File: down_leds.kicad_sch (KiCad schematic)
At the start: 9 parts, among them U5 DMG2305UX-7

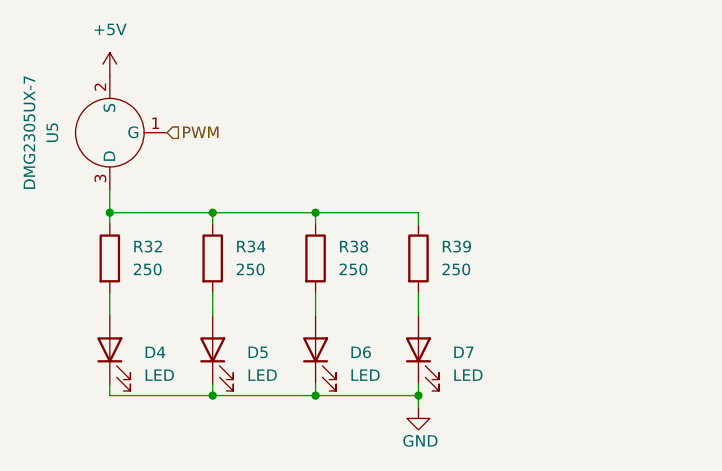
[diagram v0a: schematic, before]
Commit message: finished wiring motor drivers and moved boot button
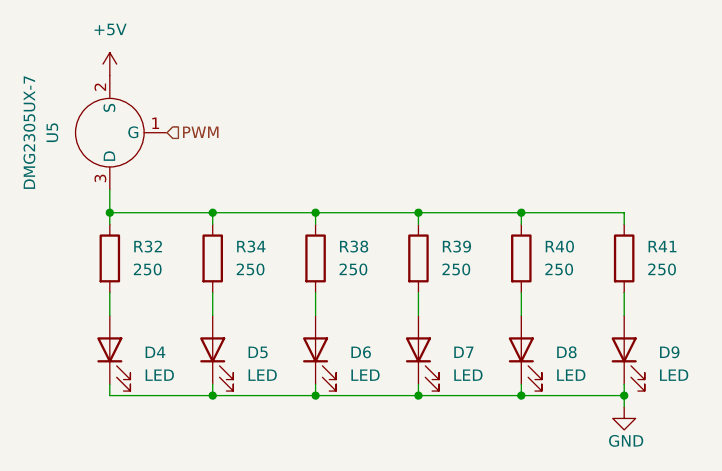
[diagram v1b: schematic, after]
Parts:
- added D8, D9: LED, LED_SMD:LED_0805_2012Metric, symbol Device:LED
- added R40, R41: 250, Resistor_SMD:R_0402_1005Metric, symbol Device:R
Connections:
- net GND: now also D8.1 (K), D9.1 (K)
- net at R32.1, R34.1, R38.1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: now also R40.1, R41.1
- new net: D9.2 (A), R41.2
- new net: D8.2 (A), R40.2

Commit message: added labels to everything
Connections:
- net DOWN_LED_DRAIN: now reaches R32.1, R34.1, R38.1, R39.1, R40.1, R41.1, U5.3 (D)
- net D6_POW: now reaches D6.2 (A), R38.2
- net D5_POW: now reaches D5.2 (A), R34.2
- net D7_POW: now reaches D7.2 (A), R39.2
- net D4_POW: now reaches D4.2 (A), R32.2
- net D9_POW: now reaches D9.2 (A), R41.2
- net D8_POW: now reaches D8.2 (A), R40.2
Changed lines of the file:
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@@
+		)
+	)
+	(label "D6_POW"
+		(at 115.57 85.09 0)
+		(effects
+			(font
+				(size 1.27 1.27)
+			)
+			(justify left bottom)
+		)
+	)
+	(label "D4_POW"
+		(at 92.71 85.09 0)
+		(effects
+			(font
+				(size 1.27 1.27)
+			)
+			(justify left bottom)
+		)
+	)
+	(label "D9_POW"
+		(at 149.86 85.09 0)
+		(effects
+			(font
+				(size 1.27 1.27)
+			)
+			(justify left bottom)
+		)
+	)
+	(label "D5_POW"
+		(at 104.14 85.09 0)
+		(effects
+			(font
+				(size 1.27 1.27)
+			)
+			(justify left bottom)
+		)
+	)
+	(label "D8_POW"
+		(at 138.43 85.09 0)
+		(effects
+			(font
+				(size 1.27 1.27)
+			)
+			(justify left bottom)
+		)
+	)
+	(label "D7_POW"
+		(at 127 85.09 0)
+		(effects
+			(font
+				(size 1.27 1.27)
+			)
+			(justify left bottom)
+		)
+	)
+	(label "DOWN_LED_DRAIN"
+		(at 95.25 73.66 0)
+		(effects
+			(font
+				(size 1.27 1.27)
+			)
+			(justify left bottom)
 		)
 	)

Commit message: more lcsc part labels for non generic components
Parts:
- U5: LCSC (none) -> C150470
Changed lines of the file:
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@@
 			)
 		)
-		(property "LCSC" ""
+		(property "LCSC" "C150470"
 			(at 92.71 64.77 90)
 			(effects

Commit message: lcsc again
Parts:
- R32, R34, R38, R39, R40, R41: LCSC (none) -> C7277389
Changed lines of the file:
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@@
+			)
+		)
+		(property "LCSC" "C7277389"
+			(at 115.57 78.74 0)
+			(effects
+				(font
+					(size 1.27 1.27)
+				)
+				(hide yes)
 			)
 		)
@@
 			)
 		)
+		(property "LCSC" "C7277389"
+			(at 92.71 78.74 0)
+			(effects
+				(font
+					(size 1.27 1.27)
+				)
+				(hide yes)
+			)
+		)
 		(pin "2"
 		)
@@
 			)
 		)
+		(property "LCSC" "C7277389"
+			(at 149.86 78.74 0)
+			(effects
+				(font
+					(size 1.27 1.27)
+				)
+				(hide yes)
+			)
+		)
 		(pin "2"
 		)
@@
 			)
 		)
+		(property "LCSC" "C7277389"
+			(at 138.43 78.74 0)
+			(effects
+				(font
+					(size 1.27 1.27)
+				)
+				(hide yes)
+			)
+		)
 		(pin "2"
 		)
@@
 			)
 		)
+		(property "LCSC" "C7277389"
+			(at 104.14 78.74 0)
+			(effects
+				(font
+					(size 1.27 1.27)
+				)
+				(hide yes)
+			)
+		)
 		(pin "2"
 		)
@@
 			(at 127 78.74 0)
 			(effects
+				(font
+					(size 1.27 1.27)
+				)
+				(hide yes)
+			)
+		)
+		(property "LCSC" "C7277389"
+			(at 127 78.74 0)
+			(effects

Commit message: changed leds
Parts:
- D4, D5, D6, D7, D8, D9: footprint LED_SMD:LED_0805_2012Metric -> LED_SMD:LED_PLCC_2835; LCSC (none) -> C2843876
- R32, R34, R38, R39, R40, R41: value 250 -> 91; footprint Resistor_SMD:R_0402_1005Metric -> Resistor_SMD:R_1206_3216Metric; LCSC C7277389 -> C5842965
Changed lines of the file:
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@@
 			)
 		)
-		(property "Value" "250"
+		(property "Value" "91"
 			(at 118.11 80.0099 0)
 			(effects
@@
 			)
 		)
-		(property "Footprint" "Resistor_SMD:R_0402_1005Metric"
+		(property "Footprint" "Resistor_SMD:R_1206_3216Metric"
 			(at 113.792 78.74 90)
 			(effects
@@
 			)
 		)
-		(property "LCSC" "C7277389"
+		(property "LCSC" "C5842965"
 			(at 115.57 78.74 0)
 			(effects
@@
 			)
 		)
-		(property "Footprint" "LED_SMD:LED_0805_2012Metric"
+		(property "Footprint" "LED_SMD:LED_PLCC_2835"
 			(at 104.14 88.9 0)
 			(effects
@@
 		(property "Sim.Pins" "1=K 2=A"
 			(at 104.14 88.9 0)
+			(effects
+				(font
+					(size 1.27 1.27)
+				)
+				(hide yes)
+			)
+		)
+		(property "LCSC" "C2843876"
+			(at 104.14 88.9 90)
 			(effects
 				(font
@@
 			)
 		)
-		(property "Footprint" "LED_SMD:LED_0805_2012Metric"
+		(property "Footprint" "LED_SMD:LED_PLCC_2835"
 			(at 127 88.9 0)
 			(effects
@@
 		(property "Sim.Pins" "1=K 2=A"
 			(at 127 88.9 0)
+			(effects
+				(font
+					(size 1.27 1.27)
+				)
+				(hide yes)
+			)
+		)
+		(property "LCSC" "C2843876"
+			(at 127 88.9 90)
 			(effects
 				(font
@@
 			)
 		)
-		(property "Footprint" "LED_SMD:LED_0805_2012Metric"
+		(property "Footprint" "LED_SMD:LED_PLCC_2835"
 			(at 115.57 88.9 0)
 			(effects
@@
 		(property "Sim.Pins" "1=K 2=A"
 			(at 115.57 88.9 0)
+			(effects
+				(font
+					(size 1.27 1.27)
+				)
+				(hide yes)
+			)
+		)
+		(property "LCSC" "C2843876"
+			(at 115.57 88.9 90)
 			(effects
 				(font
@@
 			)
 		)
-		(property "Value" "250"
+		(property "Value" "91"
 			(at 95.25 80.0099 0)
 			(effects
@@
 			)
 		)
-		(property "Footprint" "Resistor_SMD:R_0402_1005Metric"
+		(property "Footprint" "Resistor_SMD:R_1206_3216Metric"
 			(at 90.932 78.74 90)
 			(effects
@@
 			)
 		)
-		(property "LCSC" "C7277389"
+		(property "LCSC" "C5842965"
 			(at 92.71 78.74 0)
 			(effects
@@
 			)
 		)
-		(property "Footprint" "LED_SMD:LED_0805_2012Metric"
+		(property "Footprint" "LED_SMD:LED_PLCC_2835"
 			(at 149.86 88.9 0)
 			(effects
@@
 		(property "Sim.Pins" "1=K 2=A"
 			(at 149.86 88.9 0)
+			(effects
+				(font
+					(size 1.27 1.27)
+				)
+				(hide yes)
+			)
+		)
+		(property "LCSC" "C2843876"
+			(at 149.86 88.9 90)
 			(effects
 				(font
@@
 			)
 		)
-		(property "Value" "250"
+		(property "Value" "91"
 			(at 152.4 80.0099 0)
 			(effects
@@
 			)
 		)
-		(property "Footprint" "Resistor_SMD:R_0402_1005Metric"
+		(property "Footprint" "Resistor_SMD:R_1206_3216Metric"
 			(at 148.082 78.74 90)
 			(effects
@@
 			)
 		)
-		(property "LCSC" "C7277389"
+		(property "LCSC" "C5842965"
 			(at 149.86 78.74 0)
 			(effects
@@
 			)
 		)
-		(property "Value" "250"
+		(property "Value" "91"
 			(at 140.97 80.0099 0)
 			(effects
@@
 			)
 		)
-		(property "Footprint" "Resistor_SMD:R_0402_1005Metric"
+		(property "Footprint" "Resistor_SMD:R_1206_3216Metric"
 			(at 136.652 78.74 90)
 			(effects
@@
 			)
 		)
-		(property "LCSC" "C7277389"
+		(property "LCSC" "C5842965"
 			(at 138.43 78.74 0)
 			(effects
@@
 			)
 		)
-		(property "Value" "250"
+		(property "Value" "91"
 			(at 106.68 80.0099 0)
 			(effects
@@
 			)
 		)
-		(property "Footprint" "Resistor_SMD:R_0402_1005Metric"
+		(property "Footprint" "Resistor_SMD:R_1206_3216Metric"
 			(at 102.362 78.74 90)
 			(effects
@@
 			)
 		)
-		(property "LCSC" "C7277389"
+		(property "LCSC" "C5842965"
 			(at 104.14 78.74 0)
 			(effects
@@
 			)
 		)
-		(property "Value" "250"
+		(property "Value" "91"
 			(at 129.54 80.0099 0)
 			(effects
@@
 			)
 		)
-		(property "Footprint" "Resistor_SMD:R_0402_1005Metric"
+		(property "Footprint" "Resistor_SMD:R_1206_3216Metric"
 			(at 125.222 78.74 90)
 			(effects
@@
 			)
 		)
-		(property "LCSC" "C7277389"
+		(property "LCSC" "C5842965"
 			(at 127 78.74 0)
 			(effects
@@
 			)
 		)
-		(property "Footprint" "LED_SMD:LED_0805_2012Metric"
+		(property "Footprint" "LED_SMD:LED_PLCC_2835"
 			(at 138.43 88.9 0)
 			(effects
@@
 		(property "Sim.Pins" "1=K 2=A"
 			(at 138.43 88.9 0)
+			(effects
+				(font
+					(size 1.27 1.27)
+				)
+				(hide yes)
+			)
+		)
+		(property "LCSC" "C2843876"
+			(at 138.43 88.9 90)
 			(effects
 				(font
@@
 			)
 		)
-		(property "Footprint" "LED_SMD:LED_0805_2012Metric"
+		(property "Footprint" "LED_SMD:LED_PLCC_2835"
 			(at 92.71 88.9 0)
 			(effects
@@
 			(effects
 				(font
+					(size 1.27 1.27)
+				)
+				(hide yes)
+			)
+		)
+		(property "LCSC" "C2843876"
+			(at 92.71 88.9 90)
+			(effects
+				(font

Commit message: changes to fix broken stuff
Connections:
- net +5V: now also U5.3 (D); no longer U5.2 (S)
- net DOWN_LED_DRAIN: now also U5.2 (S); no longer U5.3 (D)
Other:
- moved on the sheet: U5
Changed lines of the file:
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@@
 	(symbol
 		(lib_id "Transistor_FET:DMG2305UX-7")
-		(at 92.71 64.77 180)
+		(at 92.71 64.77 0)
+		(mirror y)
 		(unit 1)
 		(body_style 1)
